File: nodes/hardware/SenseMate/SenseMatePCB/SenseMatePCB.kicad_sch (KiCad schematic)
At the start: 16 parts, among them M1 Motor_DC, Q1 2SC1815, Q2 2SC1815, SW1 SW_Push, SW2 SW_Push, SW3 SW_Push, SW5 SW_DPDT_x2

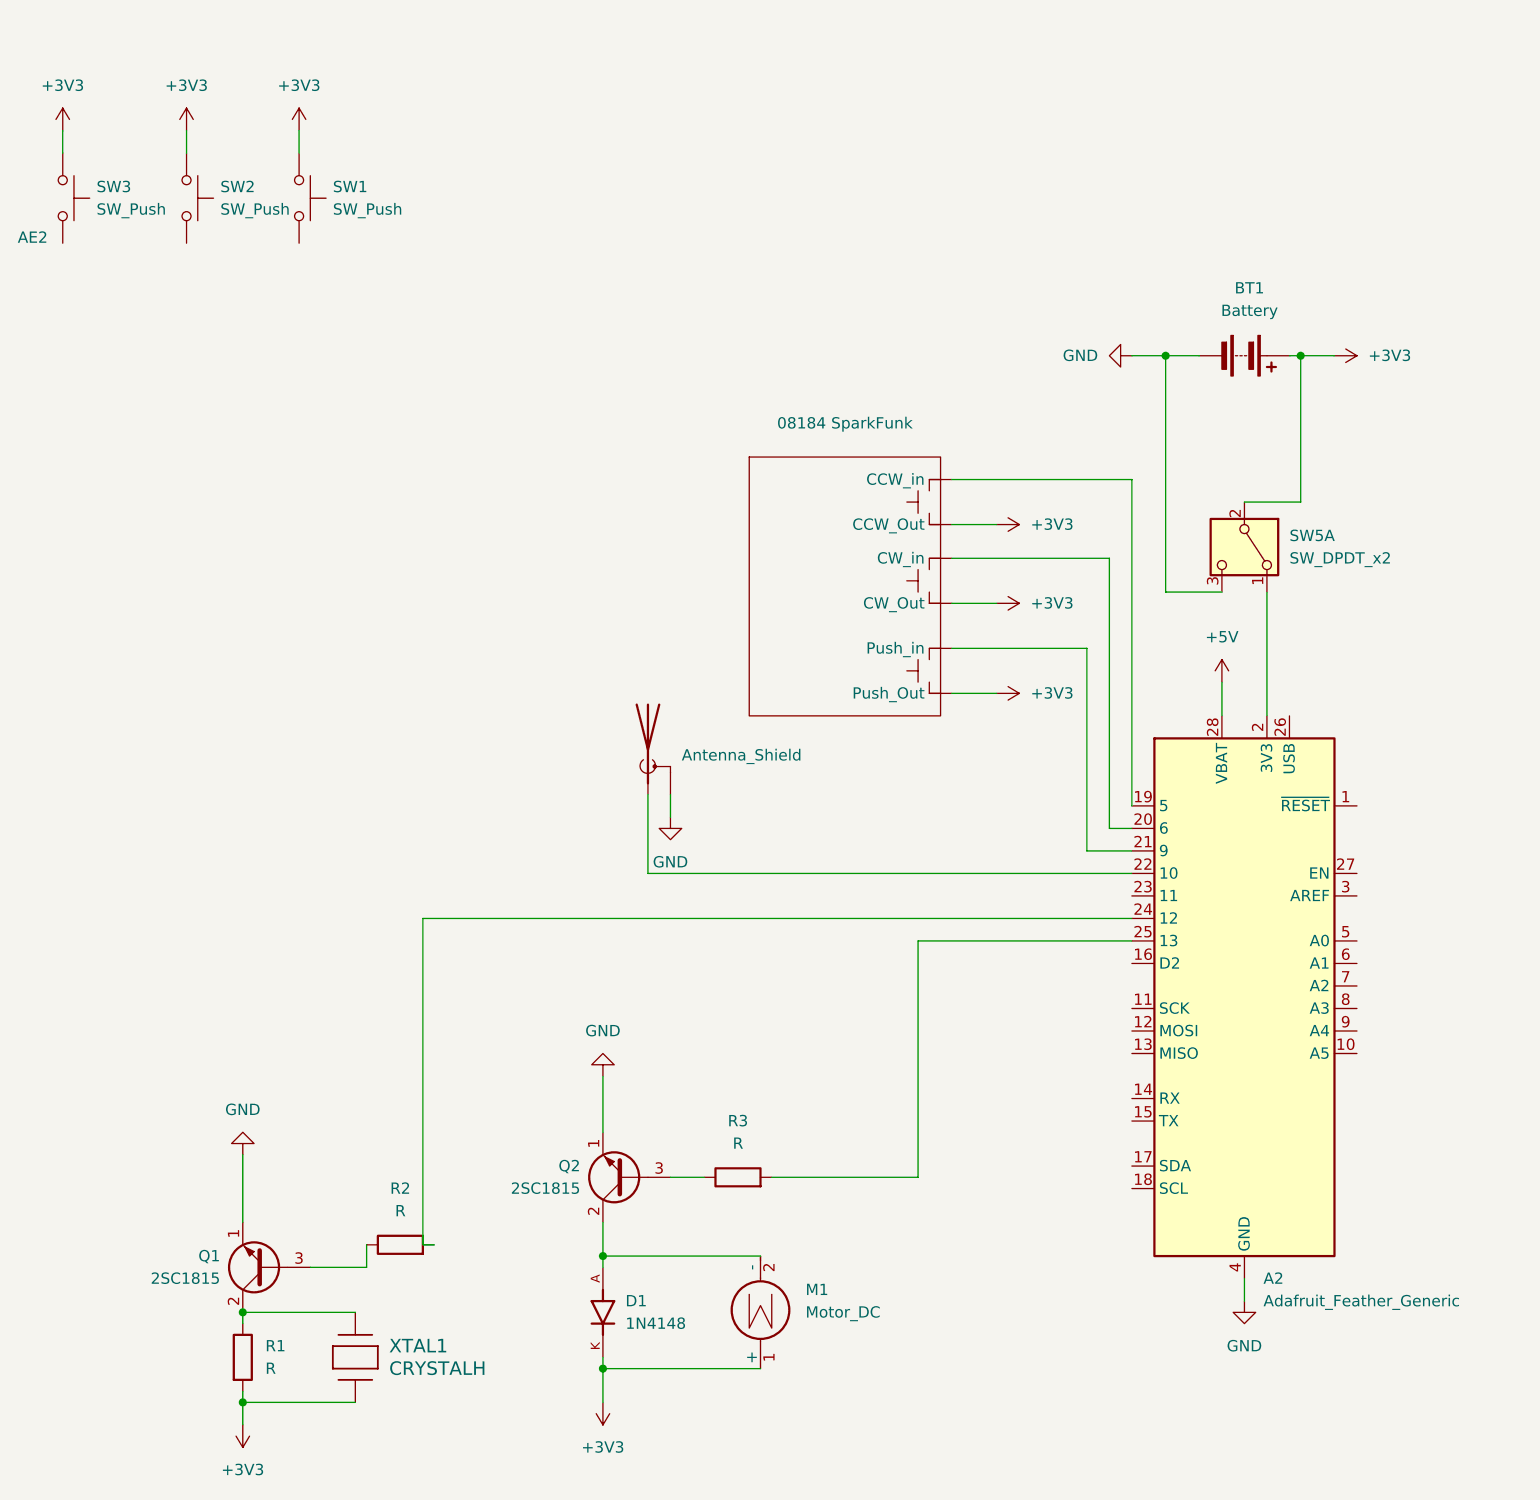
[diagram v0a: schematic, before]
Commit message: Schmatic ready for testing issue#02 (#11)
* Update GitFlow naming of bRANCHES FOR FAK HIRACHY

* Reorganized initial folder structure

* Add Readme

* Add Heading in GateMate Readme

* Add RIOT as a submodule in nodes/RIOT

* added Display and Lora Lables

* first draft for schematic finished and ready for testing

* resolved pr issues

---------

Co-authored-by: makrej <marc.siekmann@haw-hamburg.de>
Co-authored-by: makrej <makrej.git@proton.me>
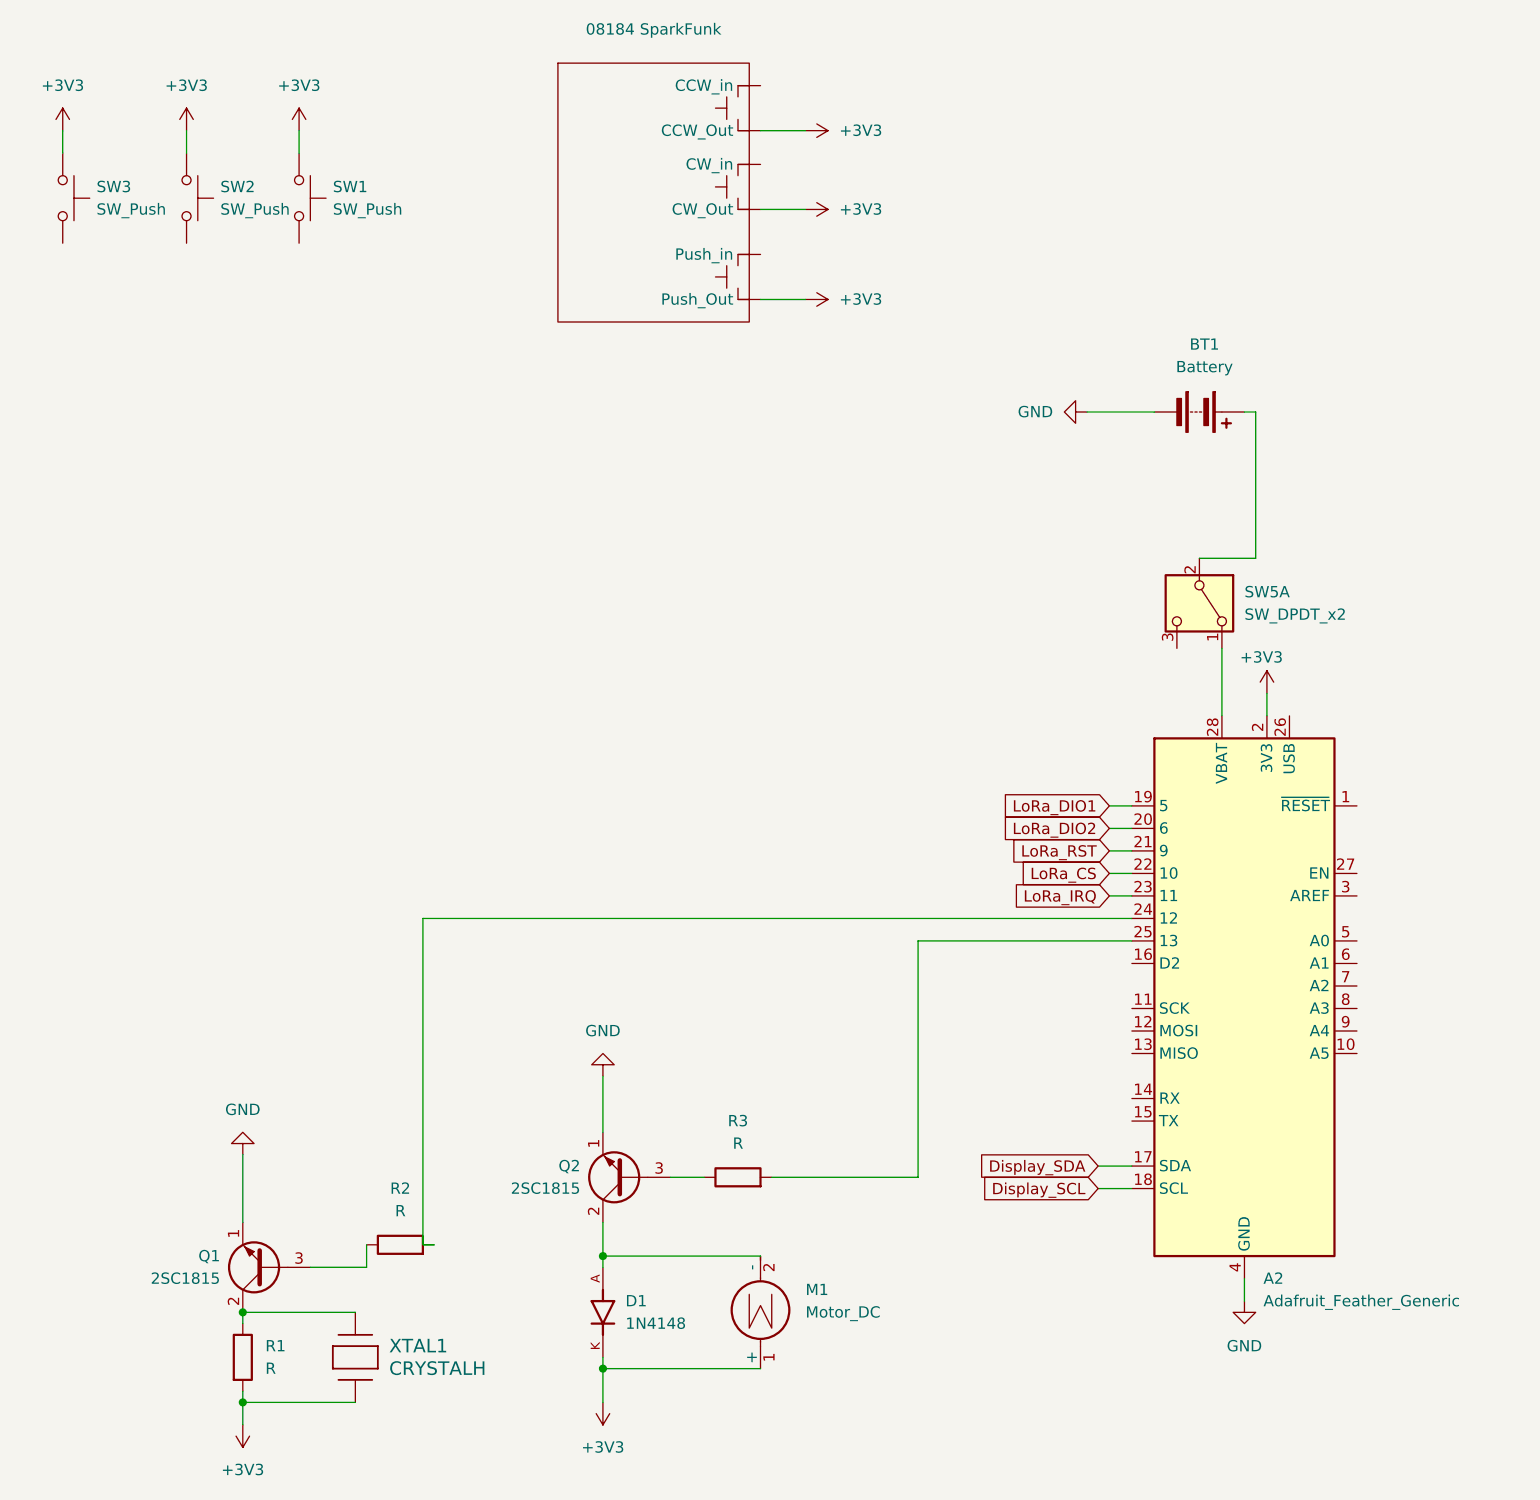
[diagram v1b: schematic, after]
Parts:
- removed AE2: Antenna_Shield, symbol Device:Antenna_Shield
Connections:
- net +5V is gone; now on an unnamed net: A2.28 (VBAT)
- net +3V3: now also A2.2 (3V3); no longer BT1.1 (+), SW5.2 (B)
- net GND: no longer SW5.3 (C)
- net LoRa_DIO1: now reaches A2.19 (5)
- net LoRa_DIO1: no longer 08184 SparkFunk. (Push_Out)
- net LoRa_DIO2: now reaches A2.20 (6)
- net LoRa_DIO2: no longer 08184 SparkFunk. (Push_Out)
- net LoRa_RST: now reaches A2.21 (9)
- net LoRa_RST: no longer 08184 SparkFunk. (Push_Out)
- net at SW5.1 (A): no longer A2.2 (3V3)
- net LoRa_CS: now reaches A2.22 (10)
- net Display_SDA: now reaches A2.17 (SDA)
- net Display_SCL: now reaches A2.18 (SCL)
- net LoRa_IRQ: now reaches A2.23 (11)
- new net: BT1.1 (+), SW5.2 (B)
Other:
- moved on the sheet: 08184 SparkFunk, BT1, SW5A
